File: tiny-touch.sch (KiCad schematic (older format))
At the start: 8 parts, among them IC1 STM32F072VBT6

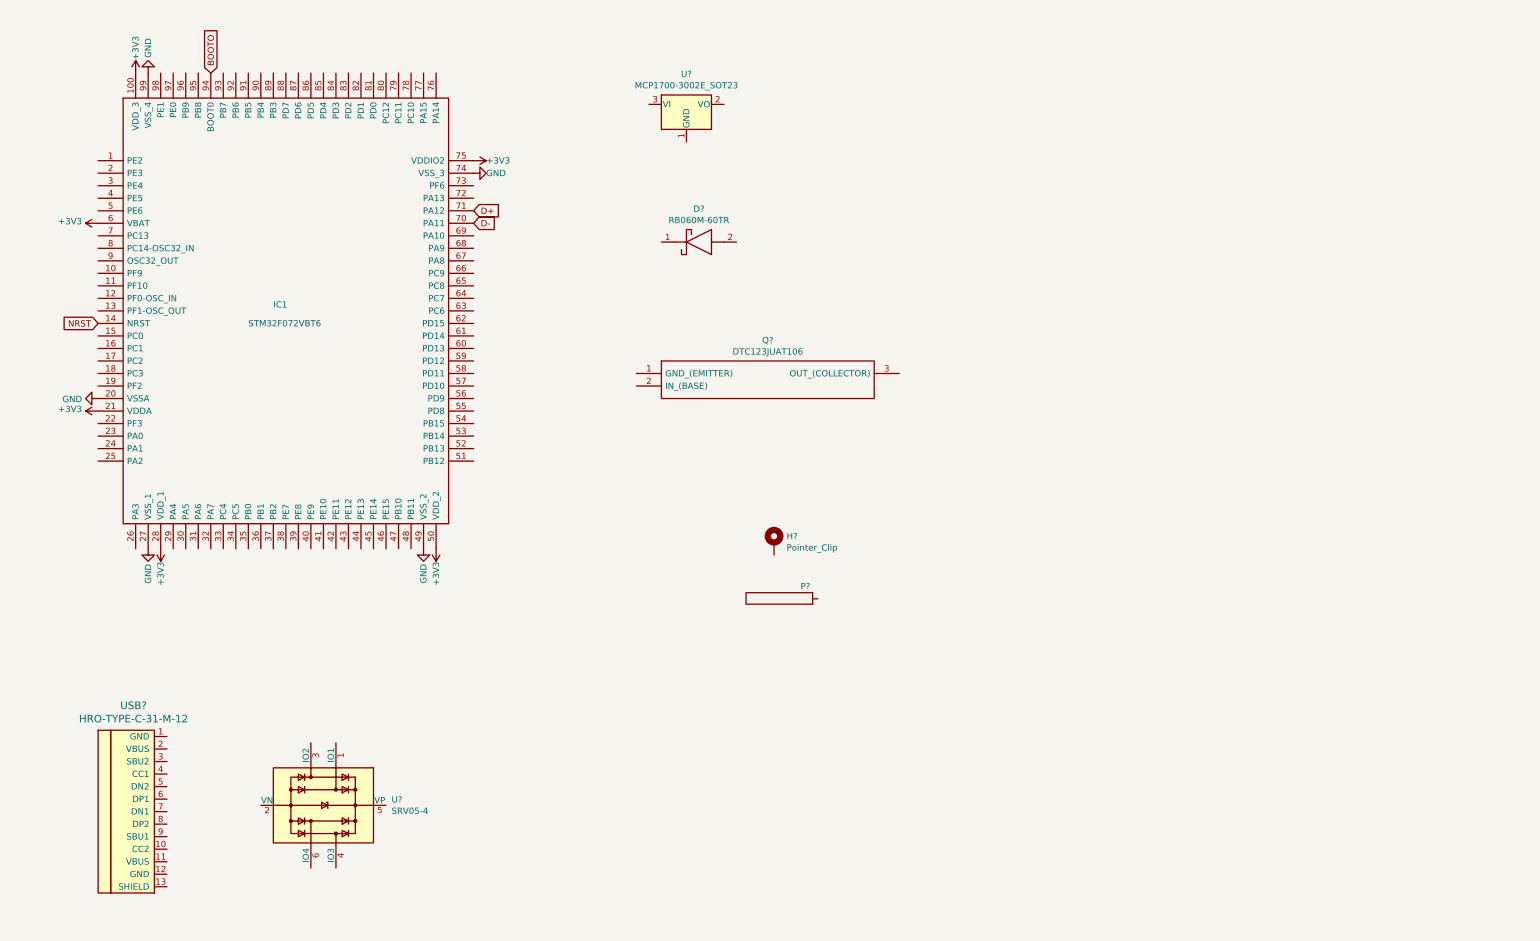
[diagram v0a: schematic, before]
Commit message: Add USB C
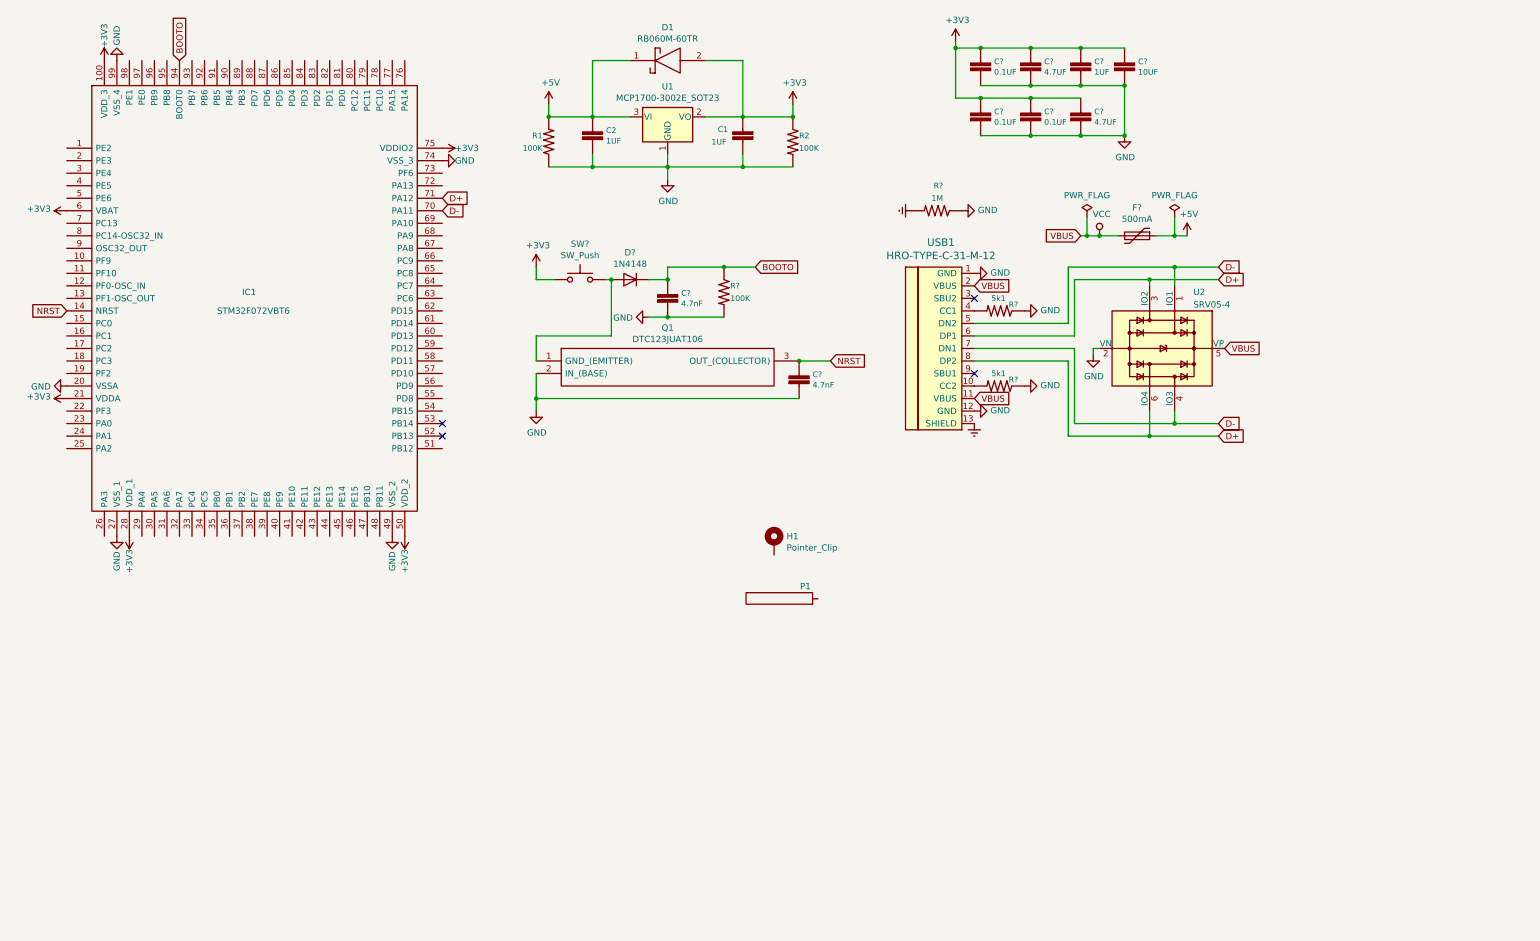
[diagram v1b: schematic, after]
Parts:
- added C1, C2, C?: 1UF, 0805, symbol SparkFun-Capacitors:1.0UF-0805-25V-_+80_-20%_
- added C? (x3): 0.1UF, 0805, symbol SparkFun-Capacitors:1.0UF-0805-25V-_+80_-20%_
- added C? (x2): 4.7UF, 0805, symbol SparkFun-Capacitors:1.0UF-0805-25V-_+80_-20%_
- added C?: 10UF, 0805, symbol SparkFun-Capacitors:1.0UF-0805-25V-_+80_-20%_
- added C? (x2): 4.7nF, 0805, symbol SparkFun-Capacitors:1.0UF-0805-25V-_+80_-20%_
- added D?: 1N4148, Diode_THT:D_DO-35_SOD27_P7.62mm_Horizontal, symbol Diode:1N4148
- added F?: 500mA, symbol Device:Polyfuse
- added R1, R2, R?: 100K, 0805, symbol SparkFun-Resistors:RESISTOR0805
- added R?: 1M, 0805, symbol SparkFun-Resistors:RESISTOR0805
- added R? (x2): 5k1, 0805, symbol SparkFun-Resistors:RESISTOR0805
- added SW?: SW_Push, symbol Switch:SW_Push
- gave numbers to parts that had none: 7
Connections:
- net +3V3: now also D1.2, U1.2 (VO), C1.2, C?.1, C?.1, C?.1, C?.1, C?.1, C?.1, C?.1, R2.1, SW?.1
- net BOOTO: now also C?.1, D?.1 (K), R?.1
- net D+: now also U2.3 (IO2), U2.6 (IO4), USB1.6 (DP1), USB1.8 (DP2)
- net D-: now also U2.1 (IO1), U2.4 (IO3), USB1.5 (DN2), USB1.7 (DN1)
- net GND: now also Q1.2 (IN_(BASE)), U1.1 (GND), U2.2 (VN), USB1.1 (GND), USB1.12 (GND), C1.1, C2.2, C?.2, C?.2, C?.2, C?.2, C?.2, C?.2, C?.2, C?.2, C?.2, R1.1, R2.2, R?.1, R?.1, R?.1, R?.2
- net NRST: now also Q1.3 (OUT_(COLLECTOR)), C?.1
- net at USB1.10 (CC2): now also R?.2
- net VCC: now reaches USB1.11 (VBUS)
- net VCC: now also U2.5 (VP), USB1.2 (VBUS), F?.2
- net GNDREF: now reaches USB1.13 (SHIELD)
- net GNDREF: now also R?.2
- net at USB1.4 (CC1): now also R?.2
- net +5V: now reaches U1.3 (VI)
- net +5V: now also D1.1, C2.1, F?.1, R1.2
- net at Q1.1 (GND_(EMITTER)): now also D?.2 (A), SW?.2
- no-connect marks 0 -> 4
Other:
- moved on the sheet: D1, IC1, Q1, U1, U2, USB1

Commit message: Re-organize schematic
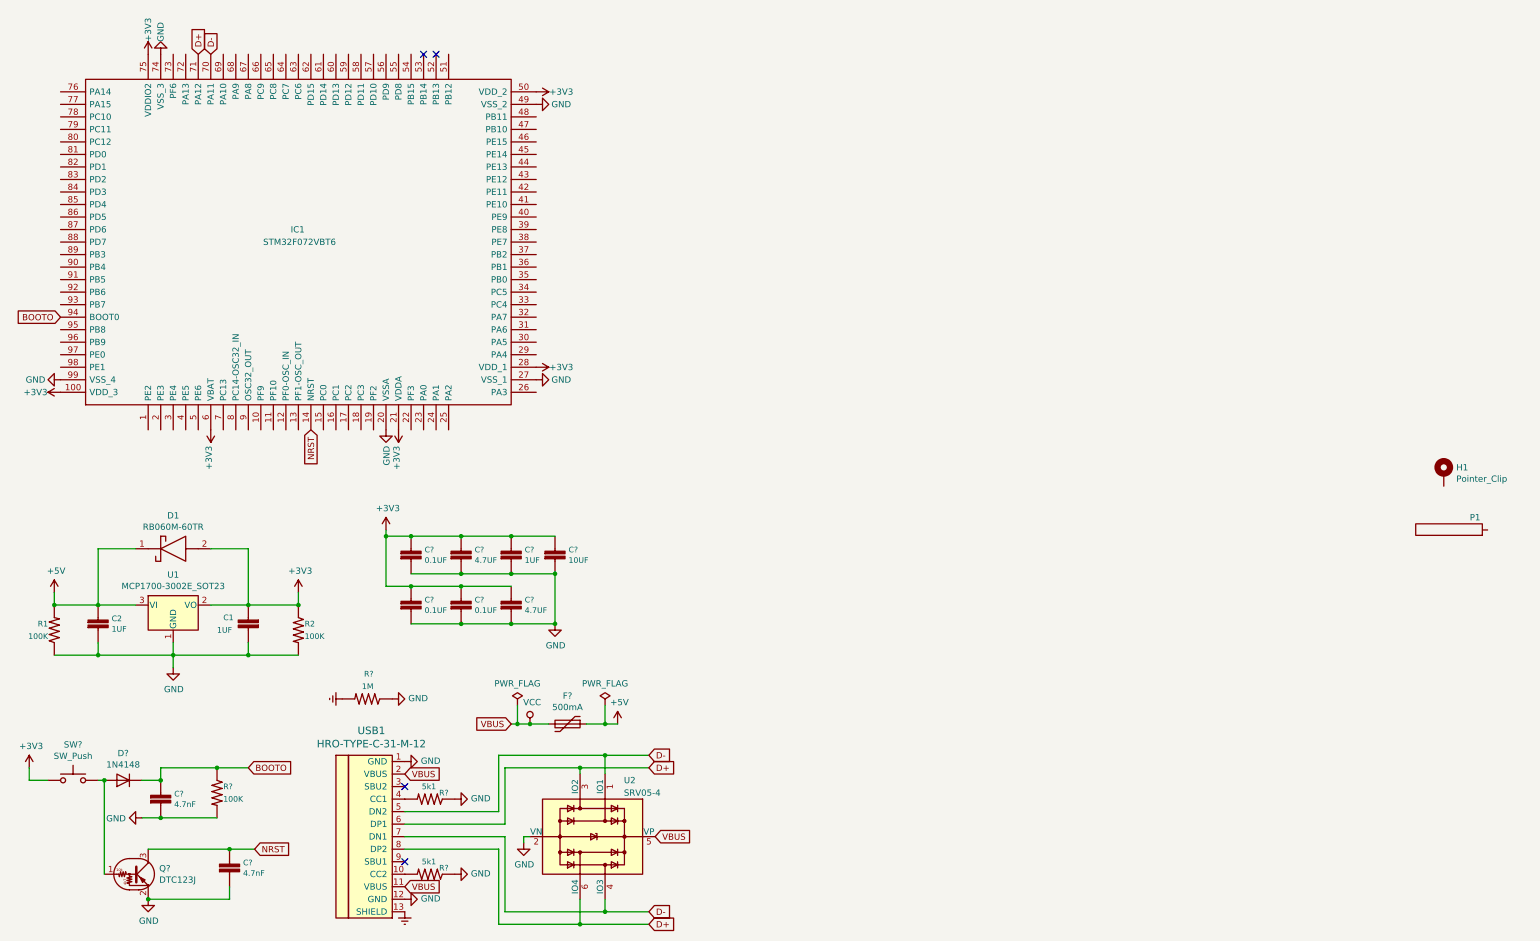
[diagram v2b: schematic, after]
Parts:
- removed Q1: DTC123JUAT106, SOT65P210X100-3N, symbol DTC123JUAT106:DTC123JUAT106
- added Q?: DTC123J, symbol Transistor_BJT:DTA114W
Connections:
- net GND: now also Q?.2 (E)
- net NRST: now also Q?.3 (C)
- net at D?.2 (A), SW?.2: now also Q?.1 (B)
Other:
- moved on the sheet: C1, C2, C?, D1, D?, F?, H1, IC1, P1, R1, R2, R?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

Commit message: Label all pins on chip
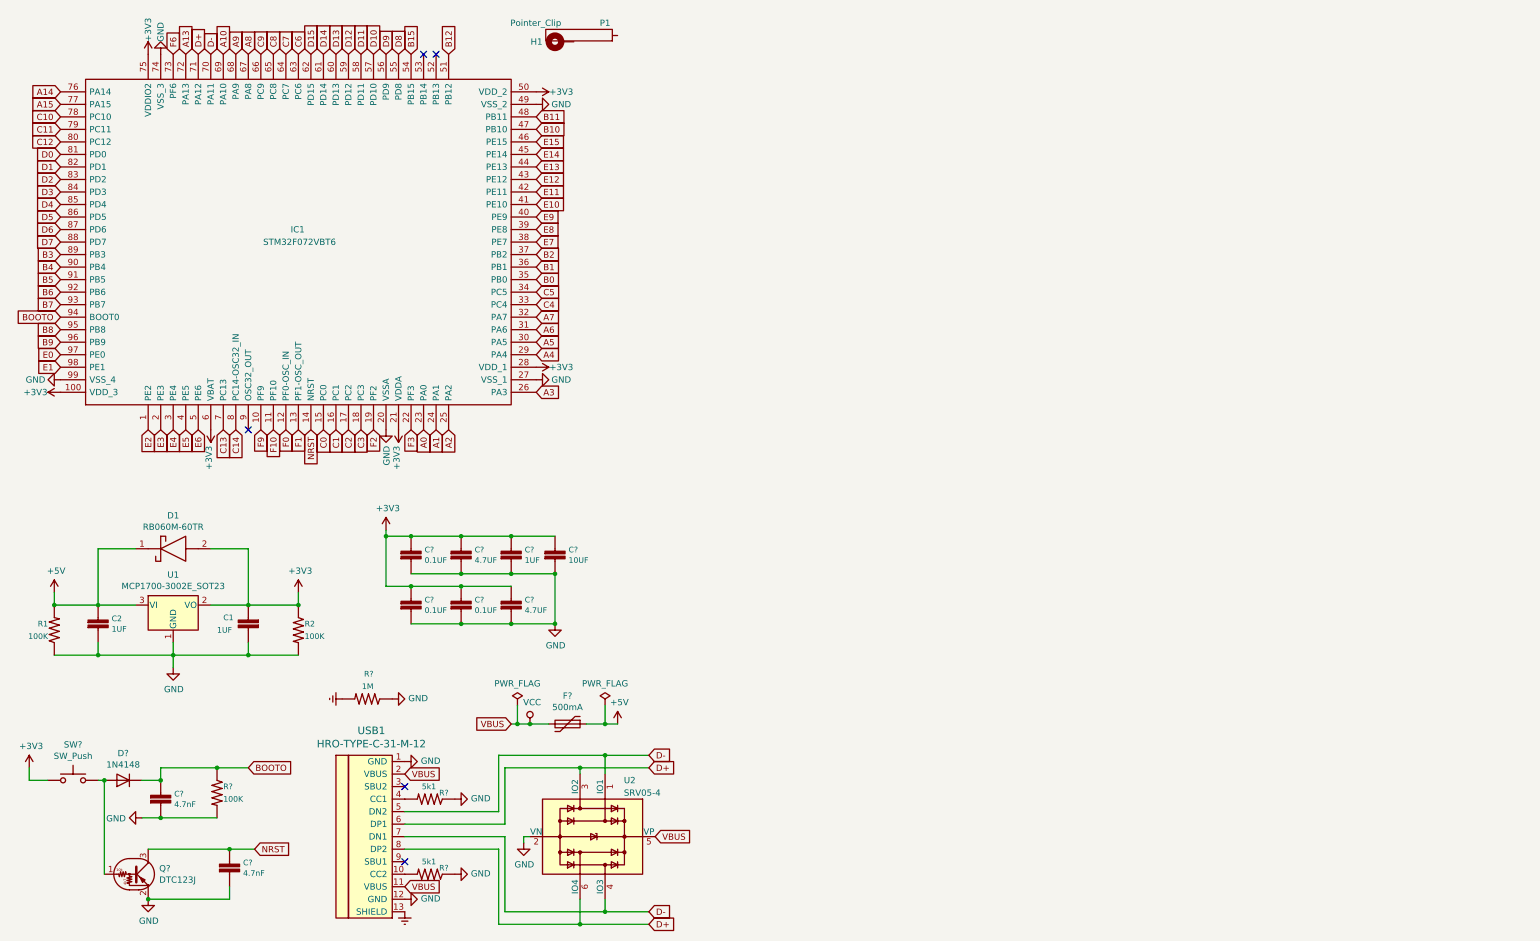
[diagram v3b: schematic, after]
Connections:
- net E2: now reaches IC1.1 (PE2)
- net F9: now reaches IC1.10 (PF9)
- net F10: now reaches IC1.11 (PF10)
- net F0: now reaches IC1.12 (PF0-OSC_IN)
- net F1: now reaches IC1.13 (PF1-OSC_OUT)
- net C0: now reaches IC1.15 (PC0)
- net C1: now reaches IC1.16 (PC1)
- net C2: now reaches IC1.17 (PC2)
- net C3: now reaches IC1.18 (PC3)
- net F2: now reaches IC1.19 (PF2)
- net E3: now reaches IC1.2 (PE3)
- net F3: now reaches IC1.22 (PF3)
- net A0: now reaches IC1.23 (PA0)
- net A1: now reaches IC1.24 (PA1)
- net A2: now reaches IC1.25 (PA2)
- net A3: now reaches IC1.26 (PA3)
- net A4: now reaches IC1.29 (PA4)
- net E4: now reaches IC1.3 (PE4)
- net A5: now reaches IC1.30 (PA5)
- net A6: now reaches IC1.31 (PA6)
- net A7: now reaches IC1.32 (PA7)
- net C4: now reaches IC1.33 (PC4)
- net C5: now reaches IC1.34 (PC5)
- net B0: now reaches IC1.35 (PB0)
- net B1: now reaches IC1.36 (PB1)
- net B2: now reaches IC1.37 (PB2)
- net E7: now reaches IC1.38 (PE7)
- net E8: now reaches IC1.39 (PE8)
- net E5: now reaches IC1.4 (PE5)
- net E9: now reaches IC1.40 (PE9)
- net E10: now reaches IC1.41 (PE10)
- net E11: now reaches IC1.42 (PE11)
- net E12: now reaches IC1.43 (PE12)
- net E13: now reaches IC1.44 (PE13)
- net E14: now reaches IC1.45 (PE14)
- net E15: now reaches IC1.46 (PE15)
- net B10: now reaches IC1.47 (PB10)
- net B11: now reaches IC1.48 (PB11)
- net E6: now reaches IC1.5 (PE6)
- net B12: now reaches IC1.51 (PB12)
- net B15: now reaches IC1.54 (PB15)
- net D8: now reaches IC1.55 (PD8)
- net D9: now reaches IC1.56 (PD9)
- net D10: now reaches IC1.57 (PD10)
- net D11: now reaches IC1.58 (PD11)
- net D12: now reaches IC1.59 (PD12)
- net D13: now reaches IC1.60 (PD13)
- net D14: now reaches IC1.61 (PD14)
- net D15: now reaches IC1.62 (PD15)
- net C6: now reaches IC1.63 (PC6)
- net C7: now reaches IC1.64 (PC7)
- net C8: now reaches IC1.65 (PC8)
- net C9: now reaches IC1.66 (PC9)
- net A8: now reaches IC1.67 (PA8)
- net A9: now reaches IC1.68 (PA9)
- net A10: now reaches IC1.69 (PA10)
- net C13: now reaches IC1.7 (PC13)
- net A13: now reaches IC1.72 (PA13)
- net F6: now reaches IC1.73 (PF6)
- net A14: now reaches IC1.76 (PA14)
- net A15: now reaches IC1.77 (PA15)
- net C10: now reaches IC1.78 (PC10)
- net C11: now reaches IC1.79 (PC11)
- net C14: now reaches IC1.8 (PC14-OSC32_IN)
- net C12: now reaches IC1.80 (PC12)
- net D0: now reaches IC1.81 (PD0)
- net D1: now reaches IC1.82 (PD1)
- net D2: now reaches IC1.83 (PD2)
- net D3: now reaches IC1.84 (PD3)
- net D4: now reaches IC1.85 (PD4)
- net D5: now reaches IC1.86 (PD5)
- net D6: now reaches IC1.87 (PD6)
- net D7: now reaches IC1.88 (PD7)
- net B3: now reaches IC1.89 (PB3)
- net B4: now reaches IC1.90 (PB4)
- net B5: now reaches IC1.91 (PB5)
- net B6: now reaches IC1.92 (PB6)
- net B7: now reaches IC1.93 (PB7)
- net B8: now reaches IC1.95 (PB8)
- net B9: now reaches IC1.96 (PB9)
- net E0: now reaches IC1.97 (PE0)
- net E1: now reaches IC1.98 (PE1)
- no-connect marks 4 -> 5
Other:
- moved on the sheet: H1, P1
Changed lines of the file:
@@
 L Mechanical:MountingHole_Pad H1
 U 1 1 5F2613A8
-P 11900 4250
-F 0 "H1" H 12000 4299 50  0000 L CNN
-F 1 "Pointer_Clip" H 12000 4208 50  0000 L CNN
-F 2 "" H 11900 4250 50  0001 C CNN
-F 3 "~" H 11900 4250 50  0001 C CNN
-	1    11900 4250
-	1    0    0    -1
+P 4850 800
+F 0 "H1" V 4850 950 50  0000 L CNN
+F 1 "Pointer_Clip" V 5000 800 50  0000 L CNN
+F 2 "" H 4850 800 50  0001 C CNN
+F 3 "~" H 4850 800 50  0001 C CNN
+	1    4850 800
+	0    -1   -1   0
 $EndComp
 $Comp
 L cKeys-symbols:Tiny-Touch-Pad P1
 U 1 1 5F25FB38
-P 12200 4700
-F 0 "P1" H 12150 4800 50  0000 C CNN
-F 1 "Tiny-Touch-Pad" H 12200 4800 50  0001 C CNN
-F 2 "" H 12200 4700 50  0001 C CNN
-F 3 "" H 12200 4700 50  0001 C CNN
-	1    12200 4700
+P 5250 750
+F 0 "P1" H 5200 850 50  0000 C CNN
+F 1 "Tiny-Touch-Pad" H 5250 850 50  0001 C CNN
+F 2 "" H 5250 750 50  0001 C CNN
+F 3 "" H 5250 750 50  0001 C CNN
+	1    5250 750
 	1    0    0    -1
 $EndComp
@@
 Wire Wire Line
 	1200 6700 1200 7450
+Text GLabel 1550 3900 3    50   Input ~ 0
+E2
+Text GLabel 1650 3900 3    50   Input ~ 0
+E3
+Text GLabel 1750 3900 3    50   Input ~ 0
+E4
+Text GLabel 1850 3900 3    50   Input ~ 0
+E5
+Text GLabel 1950 3900 3    50   Input ~ 0
+E6
+Text GLabel 2150 3900 3    50   Input ~ 0
+C13
+Text GLabel 2250 3900 3    50   Input ~ 0
+C14
+Text GLabel 2450 3900 3    50   Input ~ 0
+F9
+NoConn ~ 2350 3900
+Text GLabel 2550 3900 3    50   Input ~ 0
+F10
+Text GLabel 2650 3900 3    50   Input ~ 0
+F0
+Text GLabel 2750 3900 3    50   Input ~ 0
+F1
+Text GLabel 2950 3900 3    50   Input ~ 0
+C0
+Text GLabel 3050 3900 3    50   Input ~ 0
+C1
+Text GLabel 3150 3900 3    50   Input ~ 0
+C2
+Text GLabel 3250 3900 3    50   Input ~ 0
+C3
+Text GLabel 3350 3900 3    50   Input ~ 0
+F2
+Text GLabel 3650 3900 3    50   Input ~ 0
+F3
+Text GLabel 3750 3900 3    50   Input ~ 0
+A0
+Text GLabel 3850 3900 3    50   Input ~ 0
+A1
+Text GLabel 3950 3900 3    50   Input ~ 0
+A2
+Text GLabel 4650 3600 2    50   Input ~ 0
+A3
+Text GLabel 4650 3300 2    50   Input ~ 0
+A4
+Text GLabel 4650 3200 2    50   Input ~ 0
+A5
+Text GLabel 4650 3100 2    50   Input ~ 0
+A6
+Text GLabel 4650 1500 2    50   Input ~ 0
+B10
+Text GLabel 4650 1400 2    50   Input ~ 0
+B11
+Text GLabel 4650 1800 2    50   Input ~ 0
+E13
+Text GLabel 4650 1700 2    50   Input ~ 0
+E14
+Text GLabel 4650 1600 2    50   Input ~ 0
+E15
+Text GLabel 4650 2100 2    50   Input ~ 0
+E10
+Text GLabel 4650 2000 2    50   Input ~ 0
+E11
+Text GLabel 4650 1900 2    50   Input ~ 0
+E12
+Text GLabel 4650 2400 2    50   Input ~ 0
+E7
+Text GLabel 4650 2300 2    50   Input ~ 0
+E8
+Text GLabel 4650 2200 2    50   Input ~ 0
+E9
+Text GLabel 4650 2700 2    50   Input ~ 0
+B0
+Text GLabel 4650 2600 2    50   Input ~ 0
+B1
+Text GLabel 4650 2500 2    50   Input ~ 0
+B2
+Text GLabel 4650 3000 2    50   Input ~ 0
+A7
+Text GLabel 4650 2900 2    50   Input ~ 0
+C4
+Text GLabel 4650 2800 2    50   Input ~ 0
+C5
+Text GLabel 3250 900  1    50   Input ~ 0
+D11
+Text GLabel 3150 900  1    50   Input ~ 0
+D12
+Text GLabel 3050 900  1    50   Input ~ 0
+D13
+Text GLabel 3550 900  1    50   Input ~ 0
+D8
+Text GLabel 3450 900  1    50   Input ~ 0
+D9
+Text GLabel 3350 900  1    50   Input ~ 0
+D10
+Text GLabel 3650 900  1    50   Input ~ 0
+B15
+Text GLabel 2550 900  1    50   Input ~ 0
+C8
+Text GLabel 2450 900  1    50   Input ~ 0
+C9
+Text GLabel 2350 900  1    50   Input ~ 0
+A8
+Text GLabel 2850 900  1    50   Input ~ 0
+D15
+Text GLabel 2750 900  1    50   Input ~ 0
+C6
+Text GLabel 2650 900  1    50   Input ~ 0
+C7
+Text GLabel 2950 900  1    50   Input ~ 0
+D14
+Text GLabel 2250 900  1    50   Input ~ 0
+A9
+Text GLabel 2150 900  1    50   Input ~ 0
+A10
+Text GLabel 1850 900  1    50   Input ~ 0
+A13
+Text GLabel 1750 900  1    50   Input ~ 0
+F6
+Text GLabel 3950 900  1    50   Input ~ 0
+B12
+Text GLabel 850  1200 0    50   Input ~ 0
+A14
+Text GLabel 850  1500 0    50   Input ~ 0
+C11
+Text GLabel 850  1400 0    50   Input ~ 0
+C10
+Text GLabel 850  1300 0    50   Input ~ 0
+A15
+Text GLabel 850  1800 0    50   Input ~ 0
+D1
+Text GLabel 850  1700 0    50   Input ~ 0
+D0
+Text GLabel 850  1600 0    50   Input ~ 0
+C12
+Text GLabel 850  1900 0    50   Input ~ 0
+D2
+Text GLabel 850  2200 0    50   Input ~ 0
+D5
+Text GLabel 850  2100 0    50   Input ~ 0
+D4
+Text GLabel 850  2000 0    50   Input ~ 0
+D3
+Text GLabel 850  2500 0    50   Input ~ 0
+B3
+Text GLabel 850  2400 0    50   Input ~ 0
+D7
+Text GLabel 850  2300 0    50   Input ~ 0
+D6
+Text GLabel 850  2600 0    50   Input ~ 0
+B4
+Text GLabel 850  2900 0    50   Input ~ 0
+B7
+Text GLabel 850  2800 0    50   Input ~ 0
+B6
+Text GLabel 850  2700 0    50   Input ~ 0
+B5
+Text GLabel 850  3100 0    50   Input ~ 0
+B8
+Text GLabel 850  3400 0    50   Input ~ 0
+E1
+Text GLabel 850  3300 0    50   Input ~ 0
+E0
+Text GLabel 850  3200 0    50   Input ~ 0
+B9
 $EndSCHEMATC
